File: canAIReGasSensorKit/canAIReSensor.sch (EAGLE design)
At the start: 19 parts, among them IC1 LP2951N, IC2 AD820N, Q1 FQN1N50CI, Q2 FQN1N50CI, X1 SSW-102-02-S-D

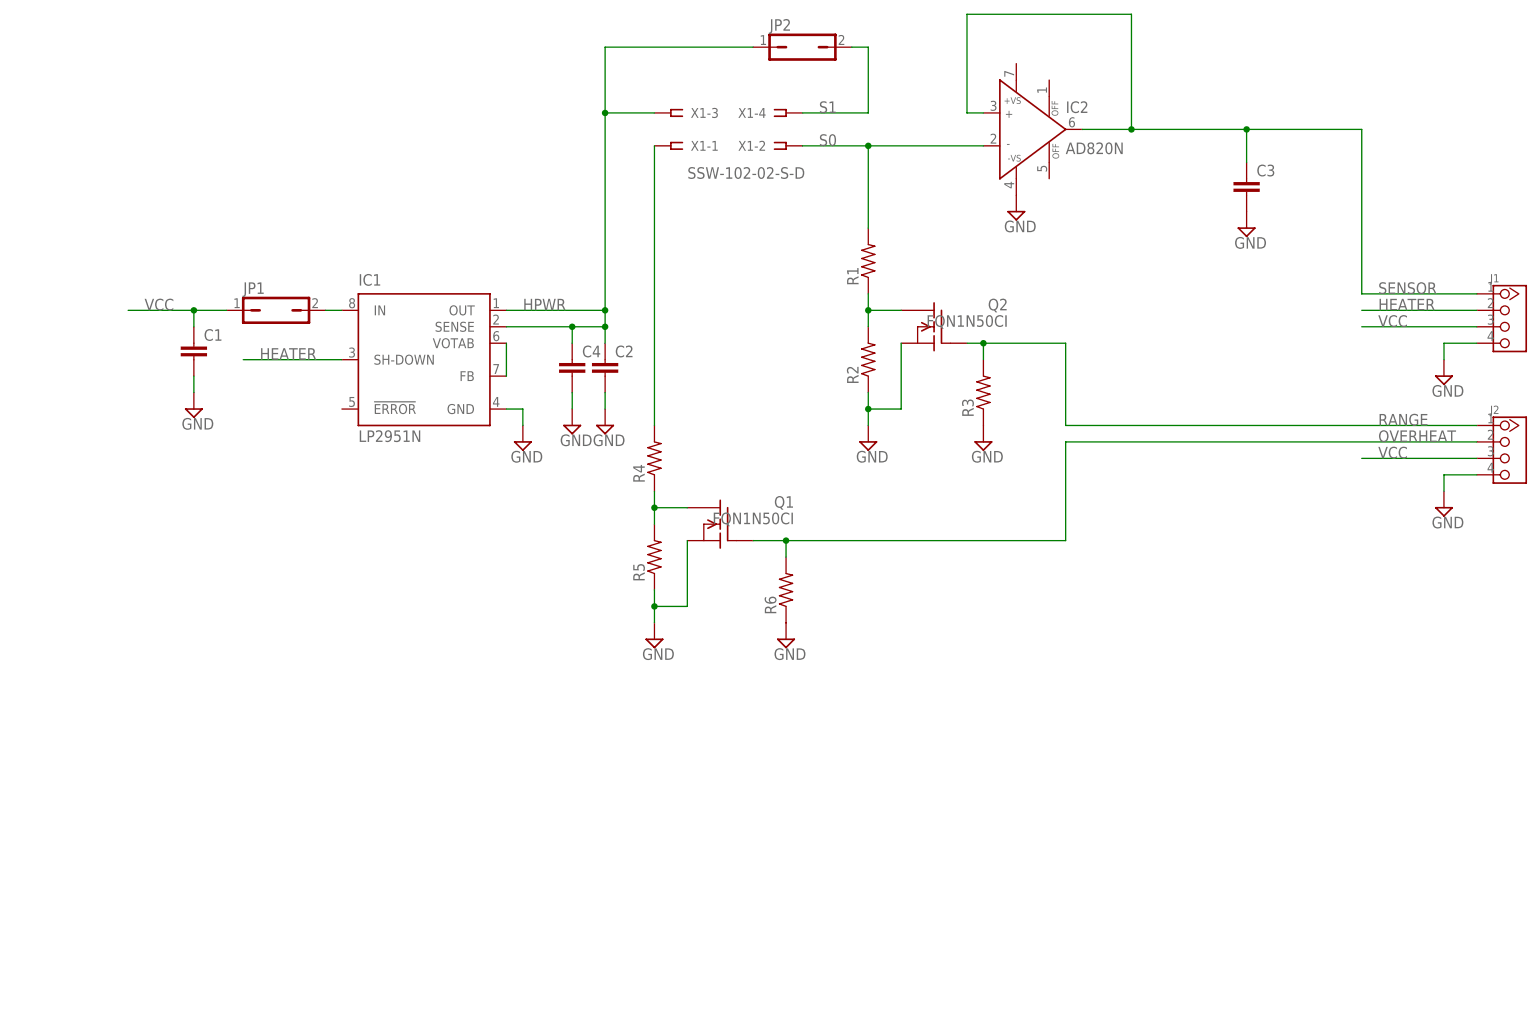
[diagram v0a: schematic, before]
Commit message: initial routing compleated
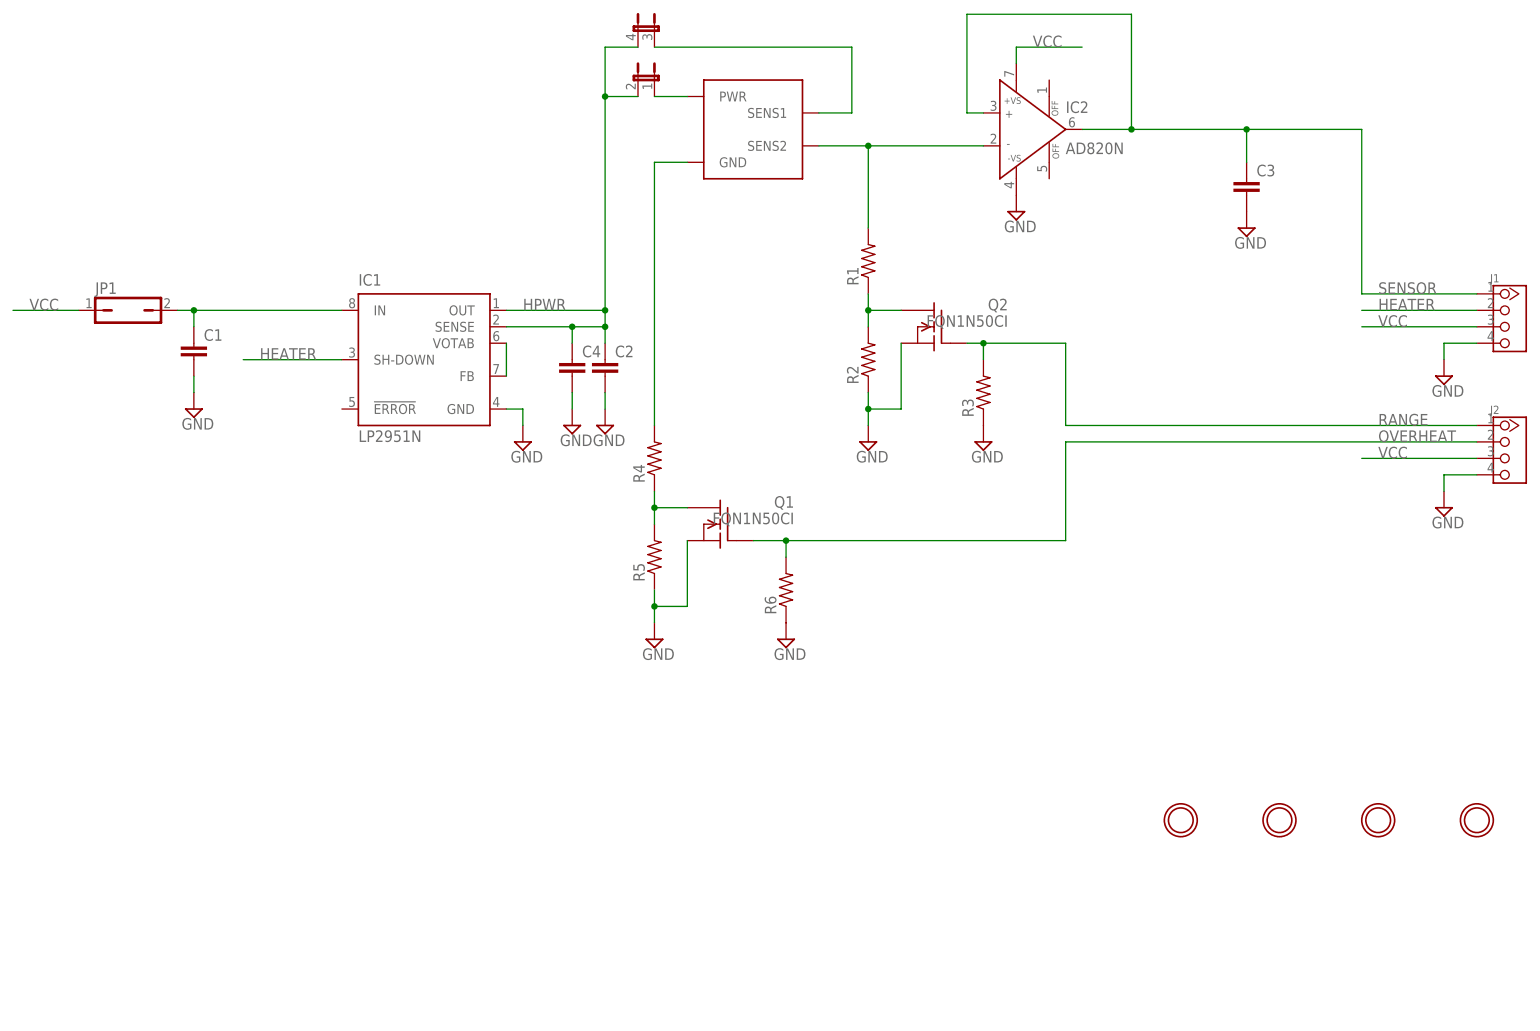
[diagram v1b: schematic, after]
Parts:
- removed JP2: (no value), jumper:JP1Q
- removed X1: SSW-102-02-S-D, con-samtec:SSW-102-02-S-D
- added JP4: (no value), jumper:JP2QE
- added U$1: E2V_MICS, open_hw_sockets:E2V_MICS
- added U$2, U$3, U$4, U$5: MOUNTINGHOLE2.5, microbuilder:MOUNTINGHOLE2.5
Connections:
- removed net S0: IC2.IN-, R1.2, X1-2.1
- removed net VIN: IC1.IN, JP1.2
- new net N$3: JP4-1.1, U$1.PWR
- new net N$5: C1.1, IC1.IN, JP1.2
- new net S2: IC2.IN-, R1.2, U$1.SENS2
- net HPWR: now also JP4-1.2, JP4-2.2; no longer JP2.1, X1-3.1
- net N$2: now also U$1.GND; no longer X1-1.1
- net S1: now also JP4-2.1, U$1.SENS1; no longer JP2.2, X1-4.1
- net VCC: now also IC2.+VS; no longer C1.1
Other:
- moved on the sheet: JP1
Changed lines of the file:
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@@
 <part name="SUPPLY2" library="supply2" deviceset="GND" device=""/>
 <part name="SUPPLY3" library="supply2" deviceset="GND" device=""/>
-<part name="X1" library="con-samtec" deviceset="SSW-102-02-S-D" device=""/>
 <part name="R1" library="rcl" deviceset="R-US_" device="0207/10"/>
 <part name="R2" library="rcl" deviceset="R-US_" device="0207/10"/>
@@
 <part name="R6" library="rcl" deviceset="R-US_" device="0207/10"/>
 <part name="SUPPLY11" library="supply2" deviceset="GND" device=""/>
-<part name="JP2" library="jumper" deviceset="JP1Q" device=""/>
 <part name="SUPPLY12" library="supply2" deviceset="GND" device=""/>
+<part name="U$1" library="open_hw_sockets" deviceset="E2V_MICS" device=""/>
+<part name="JP4" library="jumper" deviceset="JP2QE" device=""/>
+<part name="U$2" library="microbuilder" deviceset="MOUNTINGHOLE" device="2.5"/>
+<part name="U$3" library="microbuilder" deviceset="MOUNTINGHOLE" device="2.5"/>
+<part name="U$4" library="microbuilder" deviceset="MOUNTINGHOLE" device="2.5"/>
+<part name="U$5" library="microbuilder" deviceset="MOUNTINGHOLE" device="2.5"/>
 </parts>
 <sheets>
@@
 <instance part="SUPPLY2" gate="GND" x="93.98" y="101.6"/>
 <instance part="SUPPLY3" gate="GND" x="236.22" y="91.44"/>
-<instance part="X1" gate="-1" x="116.84" y="147.32" smashed="yes" rot="R180">
-<attribute name="VALUE" x="119.38" y="142.24" size="1.778" layer="96"/>
-<attribute name="NAME" x="119.888" y="146.558" size="1.524" layer="95"/>
-</instance>
-<instance part="X1" gate="-2" x="134.62" y="147.32"/>
-<instance part="X1" gate="-3" x="116.84" y="152.4" rot="R180"/>
-<instance part="X1" gate="-4" x="134.62" y="152.4"/>
 <instance part="R1" gate="G$1" x="147.32" y="129.54" rot="R90"/>
 <instance part="R2" gate="G$1" x="147.32" y="114.3" rot="R90"/>
@@
 <instance part="R4" gate="G$1" x="114.3" y="99.06" rot="R90"/>
 <instance part="R5" gate="G$1" x="114.3" y="83.82" rot="R90"/>
-<instance part="JP1" gate="A" x="55.88" y="121.92" rot="R270"/>
+<instance part="JP1" gate="A" x="33.02" y="121.92" rot="R270"/>
 <instance part="SUPPLY4" gate="GND" x="114.3" y="71.12"/>
 <instance part="SUPPLY5" gate="GND" x="43.18" y="106.68"/>
@@
 <instance part="R6" gate="G$1" x="134.62" y="78.74" rot="R90"/>
 <instance part="SUPPLY11" gate="GND" x="134.62" y="71.12"/>
-<instance part="JP2" gate="A" x="137.16" y="162.56" rot="R270"/>
 <instance part="SUPPLY12" gate="GND" x="101.6" y="104.14"/>
+<instance part="U$1" gate="G$1" x="129.54" y="149.86"/>
+<instance part="JP4" gate="-1" x="114.3" y="157.48" smashed="yes" rot="MR0">
+<attribute name="NAME" x="115.57" y="157.48" size="1.778" layer="95" rot="MR90" display="off"/>
+<attribute name="VALUE" x="108.585" y="157.48" size="1.778" layer="96" rot="MR90"/>
+</instance>
+<instance part="JP4" gate="-2" x="114.3" y="165.1" smashed="yes" rot="MR0">
+<attribute name="NAME" x="115.57" y="165.1" size="1.778" layer="95" rot="MR90" display="off"/>
+<attribute name="VALUE" x="108.585" y="165.1" size="1.778" layer="96" rot="MR90"/>
+</instance>
+<instance part="U$2" gate="G$1" x="195.58" y="43.18"/>
+<instance part="U$3" gate="G$1" x="210.82" y="43.18"/>
+<instance part="U$4" gate="G$1" x="226.06" y="43.18"/>
+<instance part="U$5" gate="G$1" x="241.3" y="43.18"/>
 </instances>
 <busses>
@@
 </segment>
 <segment>
+<pinref part="IC2" gate="G$1" pin="+VS"/>
+<wire x1="170.18" y1="160.02" x2="170.18" y2="162.56" width="0.1524" layer="91"/>
+<wire x1="170.18" y1="162.56" x2="180.34" y2="162.56" width="0.1524" layer="91"/>
+<label x="172.72" y="162.56" size="1.778" layer="95"/>
+</segment>
+<segment>
 <pinref part="JP1" gate="A" pin="1"/>
-<wire x1="48.26" y1="121.92" x2="43.18" y2="121.92" width="0.1524" layer="91"/>
-<label x="35.56" y="121.92" size="1.778" layer="95"/>
-<pinref part="C1" gate="G$1" pin="1"/>
-<wire x1="43.18" y1="121.92" x2="33.02" y2="121.92" width="0.1524" layer="91"/>
-<wire x1="43.18" y1="119.38" x2="43.18" y2="121.92" width="0.1524" layer="91"/>
-<junction x="43.18" y="121.92"/>
+<wire x1="25.4" y1="121.92" x2="15.24" y2="121.92" width="0.1524" layer="91"/>
+<label x="17.78" y="121.92" size="1.778" layer="95"/>
 </segment>
 </net>
@@
 </segment>
 </net>
-<net name="S0" class="0">
-<segment>
-<label x="139.7" y="147.32" size="1.778" layer="95"/>
-<pinref part="X1" gate="-2" pin="1"/>
-<wire x1="137.16" y1="147.32" x2="147.32" y2="147.32" width="0.1524" layer="91"/>
+<net name="S2" class="0">
+<segment>
+<wire x1="139.7" y1="147.32" x2="147.32" y2="147.32" width="0.1524" layer="91"/>
 <pinref part="R1" gate="G$1" pin="2"/>
 <wire x1="147.32" y1="147.32" x2="165.1" y2="147.32" width="0.1524" layer="91"/>
@@
 <junction x="147.32" y="147.32"/>
 <pinref part="IC2" gate="G$1" pin="IN-"/>
+<pinref part="U$1" gate="G$1" pin="SENS2"/>
 </segment>
 </net>
 <net name="HPWR" class="0">
 <segment>
-<wire x1="114.3" y1="152.4" x2="106.68" y2="152.4" width="0.1524" layer="91"/>
 <label x="93.98" y="121.92" size="1.778" layer="95"/>
-<pinref part="X1" gate="-3" pin="1"/>
 <pinref part="IC1" gate="G$1" pin="OUT"/>
 <wire x1="91.44" y1="121.92" x2="106.68" y2="121.92" width="0.1524" layer="91"/>
-<wire x1="106.68" y1="121.92" x2="106.68" y2="152.4" width="0.1524" layer="91"/>
+<wire x1="106.68" y1="121.92" x2="106.68" y2="154.94" width="0.1524" layer="91"/>
 <pinref part="IC1" gate="G$1" pin="SENSE"/>
+<wire x1="106.68" y1="154.94" x2="106.68" y2="162.56" width="0.1524" layer="91"/>
 <wire x1="91.44" y1="119.38" x2="101.6" y2="119.38" width="0.1524" layer="91"/>
 <wire x1="101.6" y1="119.38" x2="106.68" y2="119.38" width="0.1524" layer="91"/>
@@
 <junction x="106.68" y="119.38"/>
 <junction x="106.68" y="121.92"/>
-<pinref part="JP2" gate="A" pin="1"/>
-<wire x1="129.54" y1="162.56" x2="106.68" y2="162.56" width="0.1524" layer="91"/>
-<wire x1="106.68" y1="162.56" x2="106.68" y2="152.4" width="0.1524" layer="91"/>
-<junction x="106.68" y="152.4"/>
 <pinref part="C4" gate="G$1" pin="1"/>
 <wire x1="101.6" y1="116.84" x2="101.6" y2="119.38" width="0.1524" layer="91"/>
 <junction x="101.6" y="119.38"/>
+<pinref part="JP4" gate="-1" pin="2"/>
+<wire x1="111.76" y1="154.94" x2="106.68" y2="154.94" width="0.1524" layer="91"/>
+<junction x="106.68" y="154.94"/>
+<pinref part="JP4" gate="-2" pin="2"/>
+<wire x1="111.76" y1="162.56" x2="106.68" y2="162.56" width="0.1524" layer="91"/>
 </segment>
 </net>
 <net name="S1" class="0">
 <segment>
-<wire x1="137.16" y1="152.4" x2="147.32" y2="152.4" width="0.1524" layer="91"/>
-<label x="139.7" y="152.4" size="1.778" layer="95"/>
-<pinref part="X1" gate="-4" pin="1"/>
-<wire x1="147.32" y1="152.4" x2="147.32" y2="162.56" width="0.1524" layer="91"/>
-<pinref part="JP2" gate="A" pin="2"/>
-<wire x1="147.32" y1="162.56" x2="144.78" y2="162.56" width="0.1524" layer="91"/>
+<wire x1="139.7" y1="152.4" x2="144.78" y2="152.4" width="0.1524" layer="91"/>
+<wire x1="144.78" y1="152.4" x2="144.78" y2="162.56" width="0.1524" layer="91"/>
+<pinref part="U$1" gate="G$1" pin="SENS1"/>
+<pinref part="JP4" gate="-2" pin="1"/>
+<wire x1="114.3" y1="162.56" x2="144.78" y2="162.56" width="0.1524" layer="91"/>
 </segment>
 </net>
@@
 </segment>
 </net>
-<net name="VIN" class="0">
-<segment>
-<pinref part="IC1" gate="G$1" pin="IN"/>
-<pinref part="JP1" gate="A" pin="2"/>
-<wire x1="66.04" y1="121.92" x2="63.5" y2="121.92" width="0.1524" layer="91"/>
-</segment>
-</net>
 <net name="N$4" class="0">
 <segment>
@@
 <net name="N$2" class="0">
 <segment>
-<pinref part="X1" gate="-1" pin="1"/>
-<wire x1="114.3" y1="147.32" x2="114.3" y2="104.14" width="0.1524" layer="91"/>
+<wire x1="114.3" y1="144.78" x2="114.3" y2="104.14" width="0.1524" layer="91"/>
 <pinref part="R4" gate="G$1" pin="2"/>
+<pinref part="U$1" gate="G$1" pin="GND"/>
+<wire x1="119.38" y1="144.78" x2="114.3" y2="144.78" width="0.1524" layer="91"/>
 </segment>
 </net>
@@
 </segment>
 </net>
+<net name="N$3" class="0">
+<segment>
+<pinref part="JP4" gate="-1" pin="1"/>
+<pinref part="U$1" gate="G$1" pin="PWR"/>
+<wire x1="114.3" y1="154.94" x2="119.38" y2="154.94" width="0.1524" layer="91"/>
+</segment>
+</net>
+<net name="N$5" class="0">
+<segment>
+<pinref part="IC1" gate="G$1" pin="IN"/>
+<pinref part="JP1" gate="A" pin="2"/>
+<wire x1="66.04" y1="121.92" x2="43.18" y2="121.92" width="0.1524" layer="91"/>
+<pinref part="C1" gate="G$1" pin="1"/>
+<wire x1="43.18" y1="121.92" x2="40.64" y2="121.92" width="0.1524" layer="91"/>
+<wire x1="43.18" y1="119.38" x2="43.18" y2="121.92" width="0.1524" layer="91"/>
+<junction x="43.18" y="121.92"/>
+</segment>
+</net>

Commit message: bundled for fab
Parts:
- added C5: (no value), rcl:C-EU050-024X044
- added R7: 330k, rcl:R-US_0204/7
- added R8: 100, rcl:R-US_0204/7
- R1: value (none) -> 1.4k; device rcl:R-US_0207/10 -> rcl:R-US_0204/7
- R2: value (none) -> 357k; device rcl:R-US_0207/10 -> rcl:R-US_0204/7
- R3, R6: value (none) -> 10k; device rcl:R-US_0207/10 -> rcl:R-US_0204/7
- R4, R5: device rcl:R-US_0207/10 -> rcl:R-US_0204/7
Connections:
- new net N$7: IC1.!ERROR, R7.1
- new net N$9: IC2.IN-, IC2.OUT, R8.2
- net GND: now also C5.2
- net S2: now also IC2.IN+; no longer IC2.IN-
- net SENSOR: now also R8.1; no longer IC2.IN+, IC2.OUT
- net VCC: now also C5.1, R7.2
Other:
- moved on the sheet: C1, C2, C3, C4, IC1, IC2, J1, J2, JP1, Q1, Q2, R1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
